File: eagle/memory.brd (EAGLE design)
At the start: 160 x 100 mm, 31 parts, among them IC1 74LS245N, IC10 74LS138N, IC11 628512, IC12 628512, IC13 628512, IC14 628512, IC2 74LS04N, IC3 628512, IC4 628512, IC5 628512, IC6 628512, IC7 AM29F010, IC8 74LS139N, IC9 74LS08N, J1 DIN41612

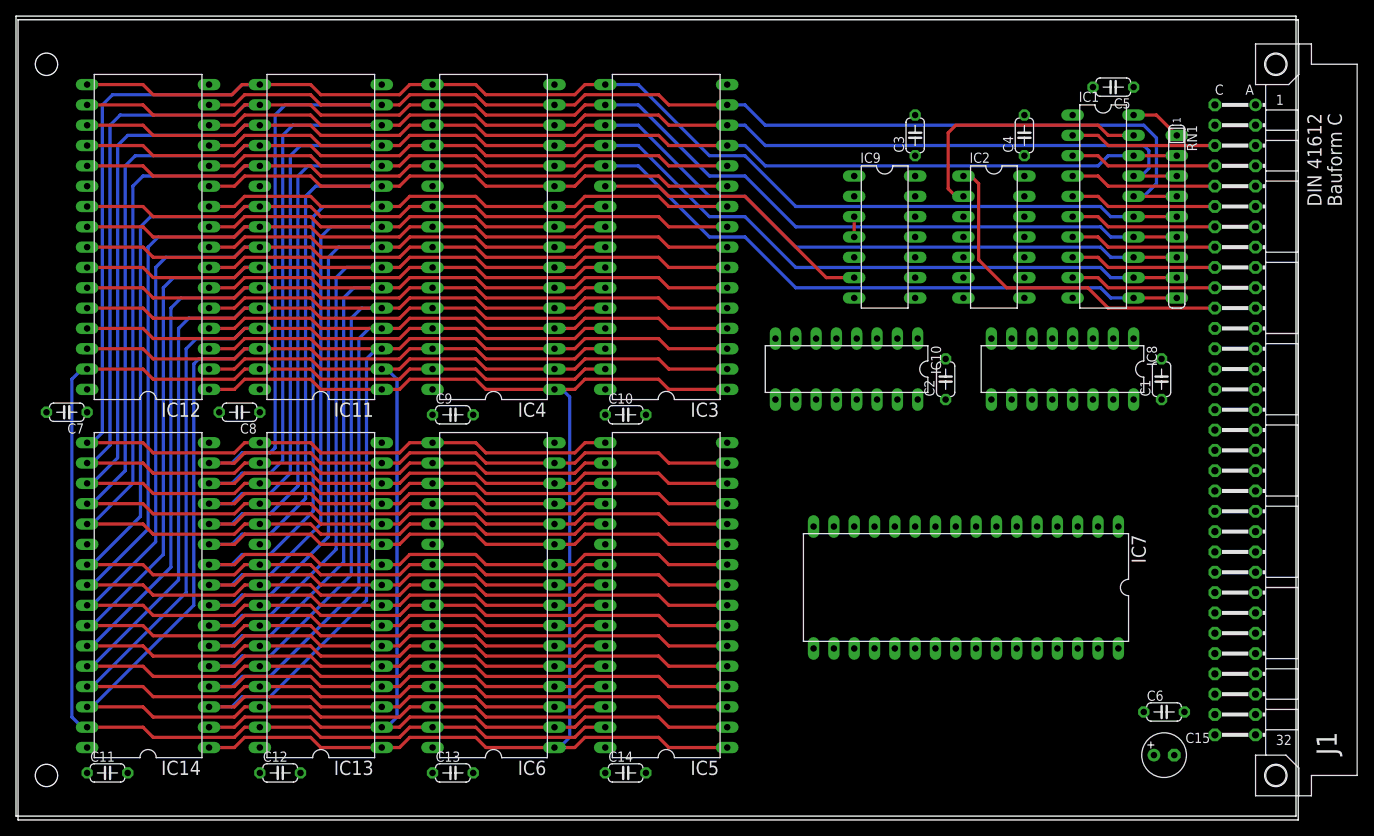
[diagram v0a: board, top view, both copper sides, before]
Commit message: Memory board v2.0 completed
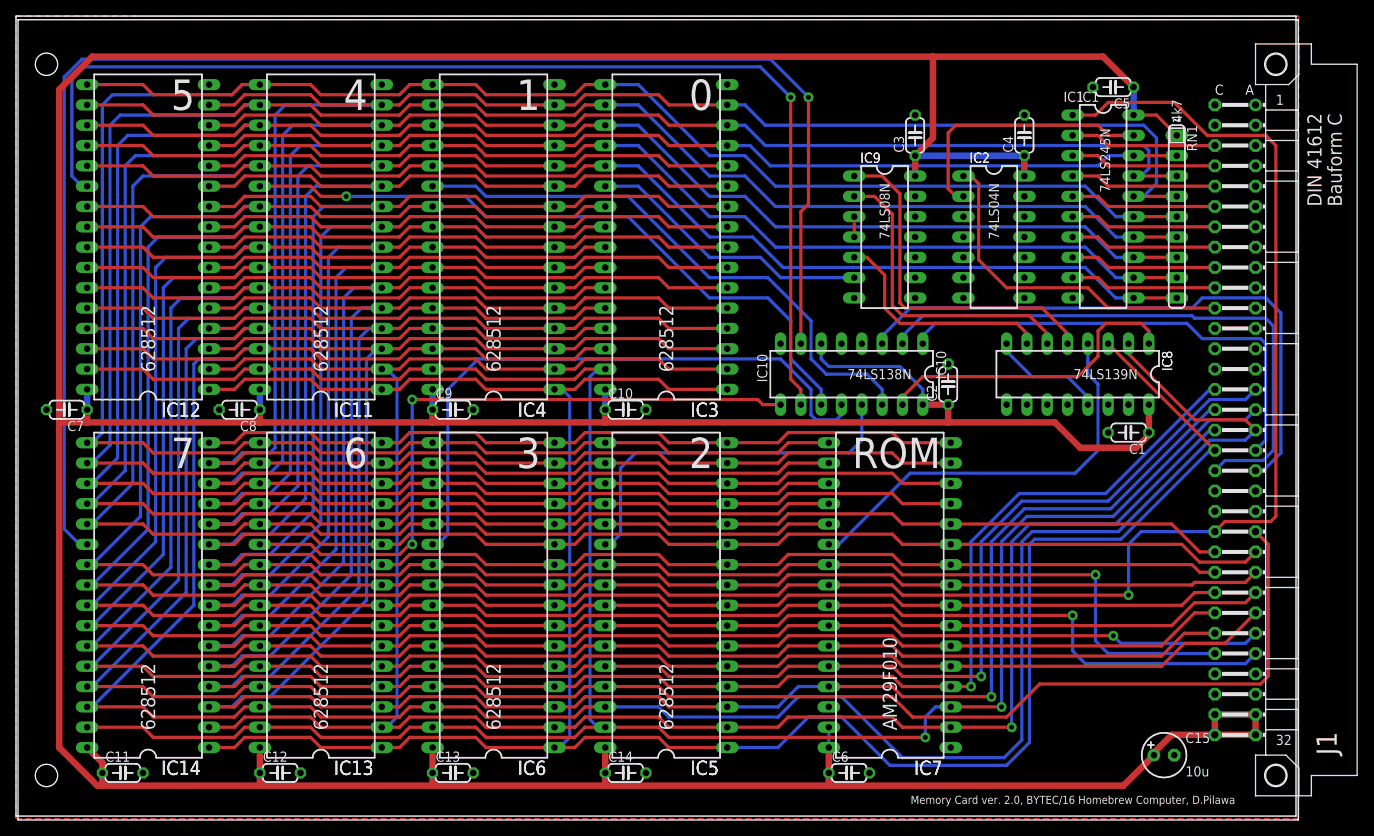
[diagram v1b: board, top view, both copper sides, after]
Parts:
- moved C6 40.1 mm to (104.1, 5.40)
- moved IC7 11.0 mm to (109.2, 26.4), turned to 90 degrees
- moved C1 7.84 mm to (139.1, 47.9), turned to 180 degrees
- moved IC8 2.01 mm to (132.7, 55.2)
- moved C11 1.91 mm to (13.3, 5.40)
- moved IC10 0.90 mm to (104.5, 55.2)
- moved C2 0.71 mm to (116.5, 54.0)
- moved C10 0.63 mm to (76.2, 50.8)
- moved C9 0.63 mm to (54.6, 50.8)
- moved C7 0.32 mm to (6.35, 50.8)
- moved C8 0.32 mm to (27.9, 50.8)
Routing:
- net +5V: track 6.45 -> 635.4 mm
- net /BANK7: track 0.00 -> 187.3 mm, vias 0 -> 1
- net /ENMEMX: track 196.6 -> 364.5 mm, vias 0 -> 1
- net /BANK5: track 0.00 -> 145.5 mm, vias 0 -> 1
- net PABUS17: track 193.7 -> 332.2 mm
- net PABUS18: track 183.1 -> 297.8 mm
- net PABUS15: track 182.9 -> 295.7 mm, vias 0 -> 2
- net GND: track 0.00 -> 111.4 mm
- net PABUS13: track 194.4 -> 302.0 mm, vias 0 -> 1
- net /LDMEMX: track 193.8 -> 299.1 mm
- net PABUS16: track 182.9 -> 273.9 mm, vias 0 -> 1
- net PABUS14: track 193.7 -> 282.4 mm, vias 0 -> 1
- net ABUS11: track 196.1 -> 284.6 mm, vias 0 -> 1
- net PABUS12: track 194.2 -> 282.2 mm, vias 0 -> 1
- net ABUS10: track 197.2 -> 283.9 mm, vias 0 -> 1
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- added copper zone on layer 1, net GND
- added copper zone on layer 16, net GND
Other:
- board text added: "0"
- board text added: "1"
- board text added: "10u"
- board text added: "2"
- board text added: "3"
- board text added: "4"
- board text added: "4k7"
- board text added: "5"
- board text added: "6"
- board text added: "628512"
- board text added: "7"
- board text added: "74LS04N"
- board text added: "74LS08N"
- board text added: "74LS138N"
- board text added: "74LS139N"
- board text added: "74LS245N"
- board text added: "AM29F010"
- board text added: "IC1"
- board text added: "IC10"
- board text added: "IC11"
- board text added: "IC12"
- board text added: "IC13"
- board text added: "IC14"
- board text added: "IC2"
- board text added: "IC3"
- board text added: "IC4"
- board text added: "IC5"
- board text added: "IC6"
- board text added: "IC7"
- board text added: "IC8"
- board text added: "IC9"
- board text added: "Memory Card ver. 2.0, BYTEC/16 Homebrew Computer, D.Pilawa"
- board text added: "ROM"
